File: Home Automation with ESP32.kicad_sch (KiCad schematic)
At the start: 32 parts, among them J1 Conn_01x04_Pin, J1 PR13-5V-450-1C, J2 Screw_Terminal_01x04, J3 Screw_Terminal_01x03, K1 RAYEX-L90AS, Q1 S8050, Q2 S8050, SW1 SW_Push, SW2 SW_Push, U1 ESP32-WROOM-32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

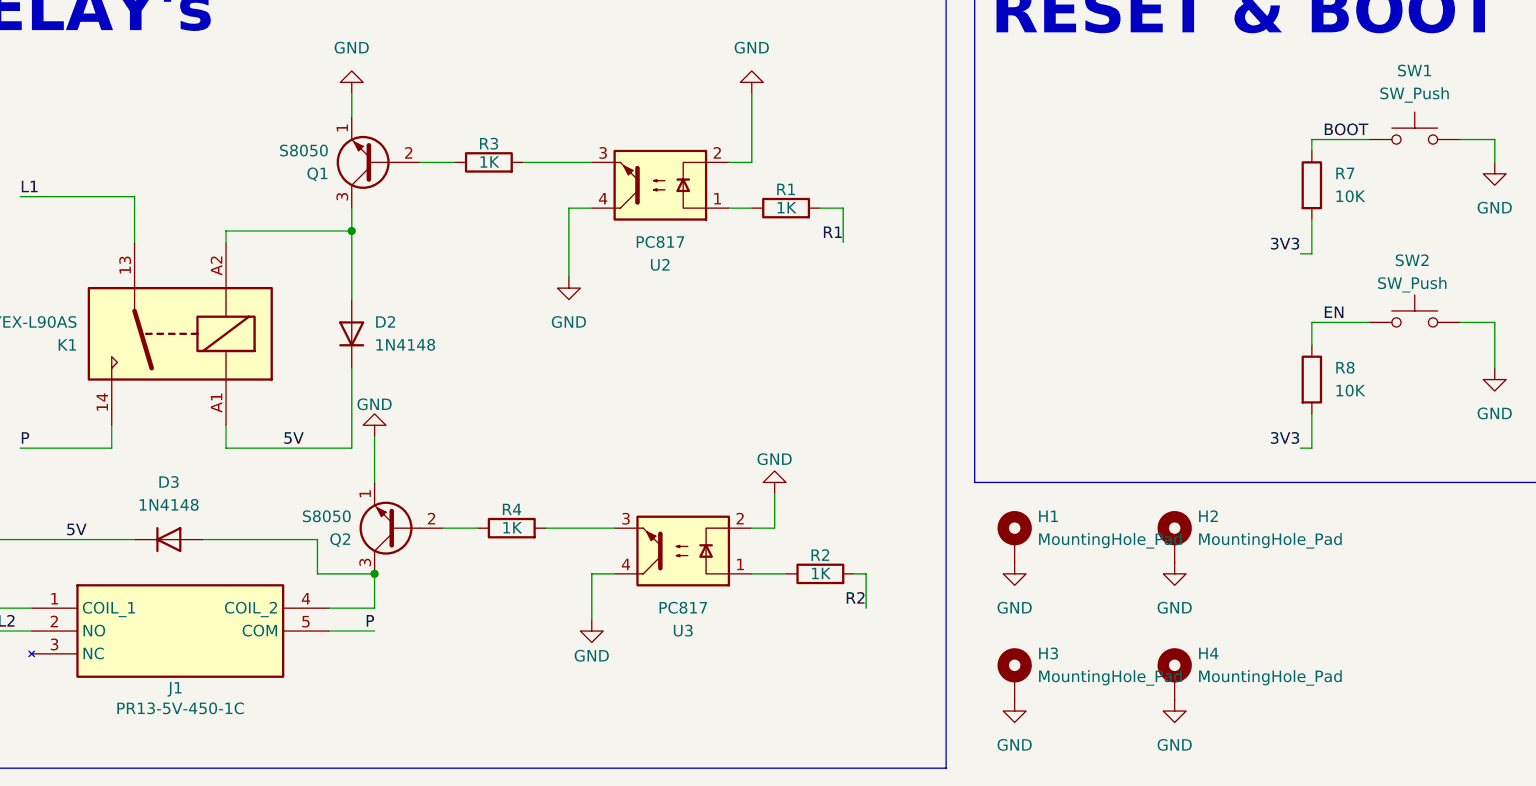
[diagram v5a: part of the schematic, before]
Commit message: assigned the footprints to in schematic
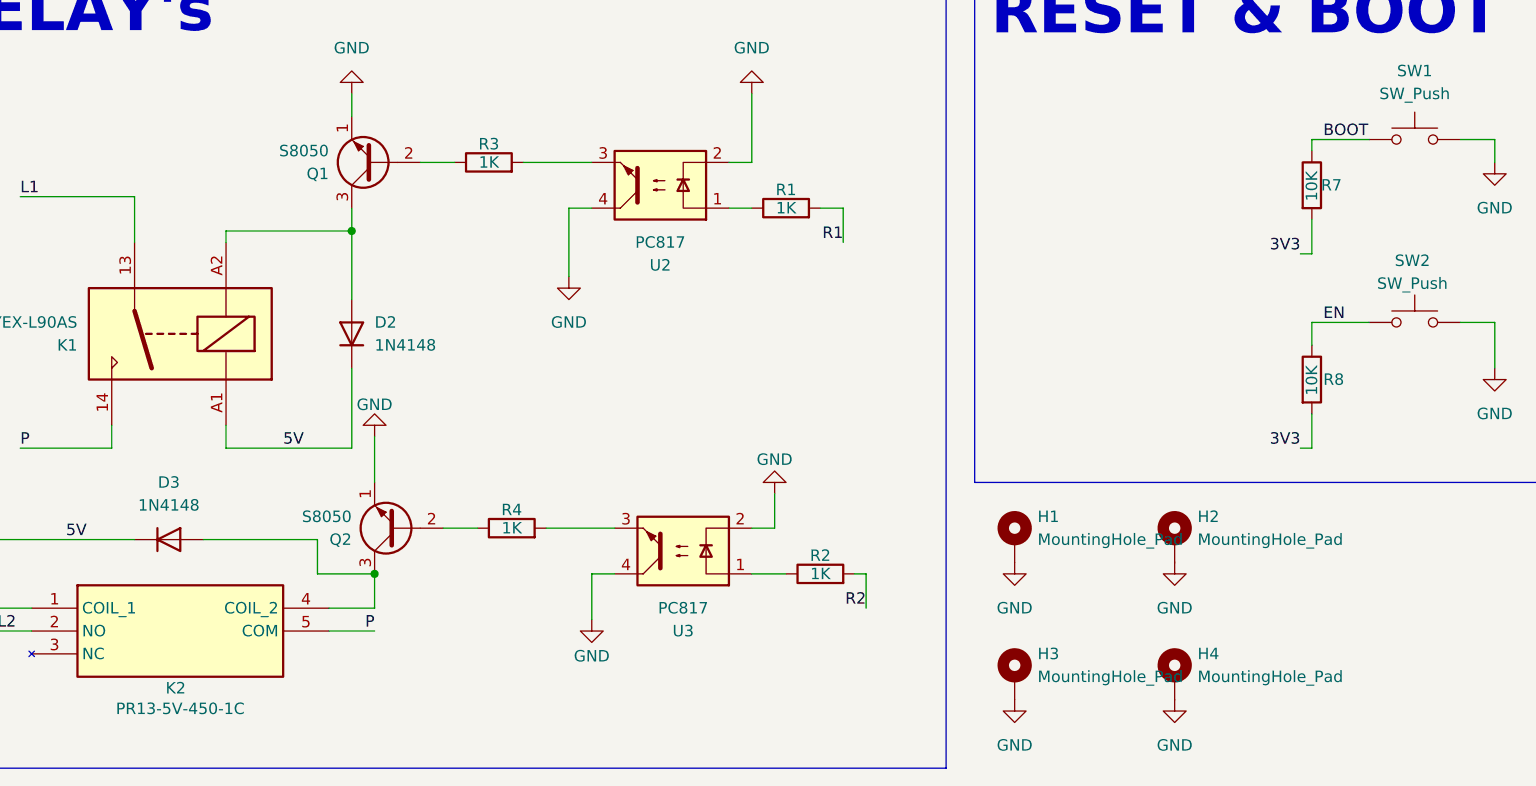
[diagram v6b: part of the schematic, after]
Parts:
- C1, C2: footprint (none) -> Capacitor_SMD:C_0805_2012Metric
- D1, D4: footprint (none) -> LED_SMD:LED_0805_2012Metric
- H1, H2, H3, H4: footprint (none) -> MountingHole:MountingHole_2.7mm_M2.5_Pad_Via
- J1: footprint (none) -> Connector_PinHeader_2.54mm:PinHeader_1x04_P2.54mm_Vertical
- J2: footprint (none) -> TerminalBlock:TerminalBlock_bornier-4_P5.08mm
- J3: footprint (none) -> TerminalBlock:TerminalBlock_bornier-3_P5.08mm
- K2: renamed from J1; footprint PR135V4501C -> Footprints:PR135V4501C
- R1, R2, R3, R4, R5, R6, R7, R8: footprint (none) -> Resistor_SMD:R_0805_2012Metric
- SW1, SW2: footprint (none) -> Button_Switch_THT:SW_PUSH_6mm
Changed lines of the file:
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@@
 			)
 		)
-		(property "Footprint" ""
+		(property "Footprint" "Connector_PinHeader_2.54mm:PinHeader_1x04_P2.54mm_Vertical"
 			(at 185.42 40.64 0)
 			(effects
@@
 			)
 		)
-		(property "Footprint" ""
+		(property "Footprint" "Button_Switch_THT:SW_PUSH_6mm"
 			(at 182.88 118.11 0)
 			(effects
@@
 			)
 		)
-		(property "Footprint" ""
+		(property "Footprint" "LED_SMD:LED_0805_2012Metric"
 			(at 184.15 76.2 0)
 			(effects
@@
 			)
 		)
-		(property "Footprint" ""
+		(property "Footprint" "MountingHole:MountingHole_2.7mm_M2.5_Pad_Via"
 			(at 138.43 167.64 0)
 			(effects
@@
 			)
 		)
-		(property "Footprint" ""
+		(property "Footprint" "MountingHole:MountingHole_2.7mm_M2.5_Pad_Via"
 			(at 138.43 182.88 0)
 			(effects
@@
 			)
 		)
-		(property "Footprint" ""
+		(property "Footprint" "Button_Switch_THT:SW_PUSH_6mm"
 			(at 182.88 138.43 0)
 			(effects
@@
 			)
 		)
-		(property "Footprint" ""
+		(property "Footprint" "Resistor_SMD:R_0805_2012Metric"
 			(at 172.72 77.978 90)
 			(effects
@@
 			)
 		)
-		(property "Footprint" ""
+		(property "Footprint" "Resistor_SMD:R_0805_2012Metric"
 			(at 80.01 127.508 90)
 			(effects
@@
 		(on_board yes)
 		(dnp no)
-		(fields_autoplaced yes)
 		(property "Reference" "R8"
-			(at 173.99 148.5899 0)
+			(at 172.72 149.86 0)
 			(effects
 				(font
@@
 		)
 		(property "Value" "10K"
-			(at 173.99 151.1299 0)
+			(at 171.45 151.638 90)
 			(effects
 				(font
@@
 			)
 		)
-		(property "Footprint" ""
+		(property "Footprint" "Resistor_SMD:R_0805_2012Metric"
 			(at 169.672 149.86 90)
 			(effects
@@
 			)
 		)
-		(property "Footprint" ""
+		(property "Footprint" "Capacitor_SMD:C_0805_2012Metric"
 			(at 84.7852 77.47 0)
 			(effects
@@
 		(on_board yes)
 		(dnp no)
-		(fields_autoplaced yes)
 		(property "Reference" "R7"
-			(at 173.99 126.9999 0)
+			(at 172.466 128.27 0)
 			(effects
 				(font
@@
 		)
 		(property "Value" "10K"
-			(at 173.99 129.5399 0)
+			(at 171.45 130.048 90)
 			(effects
 				(font
@@
 			)
 		)
-		(property "Footprint" ""
+		(property "Footprint" "Resistor_SMD:R_0805_2012Metric"
 			(at 169.672 128.27 90)
 			(effects
@@
 			)
 		)
-		(property "Footprint" ""
+		(property "Footprint" "Capacitor_SMD:C_0805_2012Metric"
 			(at 117.8052 77.47 0)
 			(effects
@@
 			)
 		)
-		(property "Footprint" ""
+		(property "Footprint" "Resistor_SMD:R_0805_2012Metric"
 			(at 116.84 173.228 90)
 			(effects
@@
 			)
 		)
-		(property "Footprint" ""
+		(property "Footprint" "MountingHole:MountingHole_2.7mm_M2.5_Pad_Via"
 			(at 156.21 167.64 0)
 			(effects
@@
 		(on_board yes)
 		(dnp no)
-		(property "Reference" "J1"
+		(property "Reference" "K2"
 			(at 45.212 184.15 0)
 			(effects
@@
 			)
 		)
-		(property "Footprint" "PR135V4501C"
+		(property "Footprint" "Footprints:PR135V4501C"
 			(at 58.42 270.18 0)
 			(effects
@@
 			(project ""
 				(path "/7438dd54-9f08-4599-aef6-4a86e3e5147b"
-					(reference "J1")
+					(reference "K2")
 					(unit 1)
 				)
@@
 			)
 		)
-		(property "Footprint" ""
+		(property "Footprint" "LED_SMD:LED_0805_2012Metric"
 			(at 184.15 86.36 0)
 			(effects
@@
 			)
 		)
-		(property "Footprint" ""
+		(property "Footprint" "TerminalBlock:TerminalBlock_bornier-4_P5.08mm"
 			(at 30.48 73.66 0)
 			(effects
@@
 			)
 		)
-		(property "Footprint" ""
+		(property "Footprint" "TerminalBlock:TerminalBlock_bornier-3_P5.08mm"
 			(at 251.46 143.51 0)
 			(effects
@@
 			)
 		)
-		(property "Footprint" ""
+		(property "Footprint" "Resistor_SMD:R_0805_2012Metric"
 			(at 172.72 88.138 90)
 			(effects
@@
 			)
 		)
-		(property "Footprint" ""
+		(property "Footprint" "Resistor_SMD:R_0805_2012Metric"
 			(at 82.55 168.148 90)
 			(effects
@@
 			)
 		)
-		(property "Footprint" ""
+		(property "Footprint" "Resistor_SMD:R_0805_2012Metric"
 			(at 113.03 132.588 90)
 			(effects
@@
 			)
 		)
-		(property "Footprint" ""
+		(property "Footprint" "MountingHole:MountingHole_2.7mm_M2.5_Pad_Via"
 			(at 156.21 182.88 0)
 			(effects
